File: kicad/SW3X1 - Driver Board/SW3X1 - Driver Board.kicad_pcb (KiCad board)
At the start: 2 copper layers, 124.5 x 66 mm, 39 parts, among them J4 locked, J5 locked, J6 locked, J7 locked, U2 locked

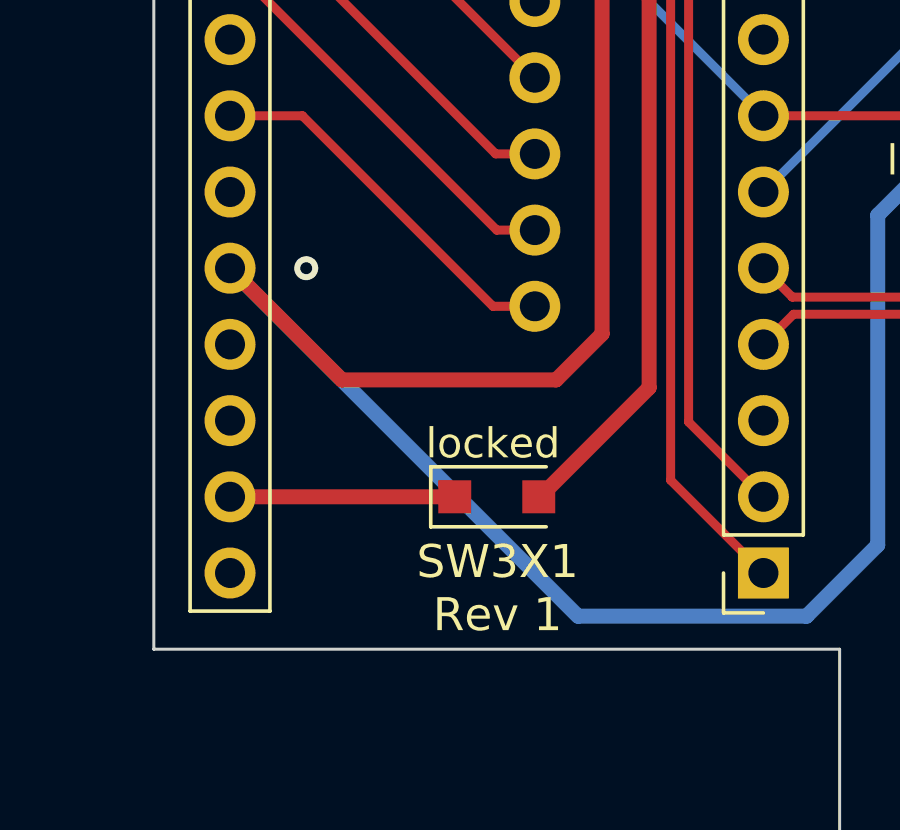
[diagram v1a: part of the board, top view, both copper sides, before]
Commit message: add USB marker for pico
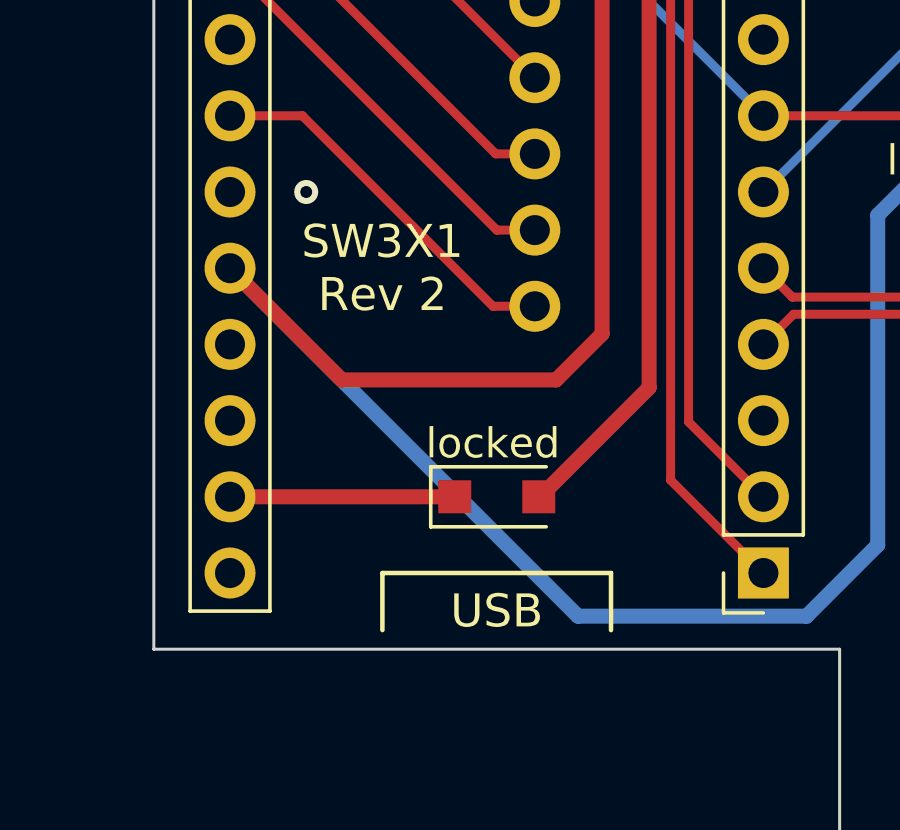
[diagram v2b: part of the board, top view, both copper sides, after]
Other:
- board text added: "SW3X1 Rev 2"
- board text added: "USB"
- board text removed: "SW3X1 Rev 1"
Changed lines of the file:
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@@
   (title_block
     (title "SW3X1 - Driver Board")
-    (date "2022-11-04")
-    (rev "1")
+    (date "2022-12-21")
+    (rev "2")
     (company "saawsm")
   )
@@
   (gr_line locked (start 146.11 107.95) (end 145.475 107.95) (layer "B.SilkS") (width 0.15))
   (gr_line locked (start 135.95 107.95) (end 135.315 107.95) (layer "B.SilkS") (width 0.15))
+  (gr_line locked (start 81.28 113.665) (end 81.28 111.76) (layer "F.SilkS") (width 0.15))
+  (gr_line locked (start 81.28 111.76) (end 88.9 111.76) (layer "F.SilkS") (width 0.15))
+  (gr_line locked (start 88.9 111.76) (end 88.9 113.665) (layer "F.SilkS") (width 0.15))
   (gr_line locked (start 73.66 54.61) (end 73.66 114.3) (layer "Edge.Cuts") (width 0.1))
   (gr_line locked (start 198.12 54.61) (end 73.66 54.61) (layer "Edge.Cuts") (width 0.1))
@@
   (gr_line locked (start 198.12 120.65) (end 198.12 54.61) (layer "Edge.Cuts") (width 0.1))
   (gr_line locked (start 73.66 114.3) (end 96.52 114.3) (layer "Edge.Cuts") (width 0.1))
-  (gr_text "SW3X1\nRev 1" (at 85.11832 112.26977) (layer "F.SilkS")
+  (gr_text "SW3X1\nRev 2" (at 81.28 101.6) (layer "F.SilkS")
     (effects (font (size 1.1 1.1) (thickness 0.2)))
   )
   (gr_text "JLCJLCJLCJLC" (at 174.272213 105.158009) (layer "F.SilkS")
     (effects (font (size 1 1) (thickness 0.15)))
+  )
+  (gr_text "USB" (at 85.09 113.03) (layer "F.SilkS")
+    (effects (font (size 1.1 1.1) (thickness 0.2)))
   )
   (dimension locked (type orthogonal) (layer "Dwgs.User")
@@
   (via locked (at 136.267903 87.529039) (size 0.8) (drill 0.4) (layers "F.Cu" "B.Cu") (free) (net 2))
   (via locked (at 138.176 92.964) (size 0.8) (drill 0.4) (layers "F.Cu" "B.Cu") (free) (net 2))
-  (via locked (at 78.74 101.6) (size 0.8) (drill 0.4) (layers "F.Cu" "B.Cu") (free) (net 2))
+  (via locked (at 78.74 99.06) (size 0.8) (drill 0.4) (layers "F.Cu" "B.Cu") (free) (net 2))
   (via locked (at 169.092155 106.464677) (size 0.8) (drill 0.4) (layers "F.Cu" "B.Cu") (free) (net 2))
   (via locked (at 132.842 84.074) (size 0.8) (drill 0.4) (layers "F.Cu" "B.Cu") (free) (net 2))
